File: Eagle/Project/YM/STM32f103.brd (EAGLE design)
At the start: 174.2 x 86.5 mm, 81 parts, among them IC1 YM3812, IC10 YM3812, IC11 YM3014B, IC12 OPA2134, IC14 74ALS04N, IC15 6N136, IC2 YM3014B, IC3 OPA2134, IC4 YM3812, IC5 YM3014B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

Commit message: gerber files
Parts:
- moved SL9 0.13 mm to (66.7, 9.65), flipped to the top, turned to 0 degrees
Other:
- board size 174.2 x 86.5 mm -> 174.6 x 86.4 mm
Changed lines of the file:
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@@
 <setting verticaltext="up"/>
 </settings>
-<grid distance="5" unitdist="mil" unit="mil" style="lines" multiple="1" display="yes" altdistance="5" altunitdist="mil" altunit="mil"/>
+<grid distance="25" unitdist="mil" unit="mil" style="lines" multiple="1" display="yes" altdistance="5" altunitdist="mil" altunit="mil"/>
 <layers>
 <layer number="1" name="Top" color="4" fill="1" visible="yes" active="yes"/>
@@
 <board>
 <plain>
-<wire x1="0" y1="0" x2="174.224" y2="0" width="0" layer="20" grouprefs="ASD"/>
-<wire x1="174.224" y1="0" x2="174.224" y2="86.538" width="0" layer="20" grouprefs="ASD"/>
-<wire x1="174.224" y1="86.538" x2="0" y2="86.538" width="0" layer="20" grouprefs="ASD"/>
-<wire x1="0" y1="86.538" x2="0" y2="0" width="0" layer="20"/>
+<wire x1="0" y1="0" x2="174.625" y2="0" width="0" layer="20" grouprefs="ASD"/>
+<wire x1="174.625" y1="0" x2="174.625" y2="86.36" width="0" layer="20" grouprefs="ASD"/>
+<wire x1="174.625" y1="86.36" x2="0" y2="86.36" width="0" layer="20" grouprefs="ASD"/>
+<wire x1="0" y1="86.36" x2="0" y2="0" width="0" layer="20"/>
 <hole x="172.212" y="84.582" drill="3.2004"/>
 <hole x="172.212" y="2.032" drill="3.2004"/>
@@
 <attribute name="VALUE" x="32.004" y="15.2146" size="1.27" layer="27" ratio="10"/>
 </element>
-<element name="SL9" library="con-amp-quick" library_urn="urn:adsk.eagle:library:125" package="06P" package3d_urn="urn:adsk.eagle:package:5960/1" value="" x="66.675" y="9.525" smashed="yes" rot="MR180">
-<attribute name="MF" value="" x="66.675" y="9.525" size="1.778" layer="28" rot="MR180" display="off"/>
-<attribute name="MPN" value="" x="66.675" y="9.525" size="1.778" layer="28" rot="MR180" display="off"/>
-<attribute name="NAME" x="59.436" y="12.2174" size="1.27" layer="25" ratio="10"/>
-<attribute name="OC_FARNELL" value="unknown" x="66.675" y="9.525" size="1.778" layer="28" rot="MR180" display="off"/>
-<attribute name="OC_NEWARK" value="unknown" x="66.675" y="9.525" size="1.778" layer="28" rot="MR180" display="off"/>
-<attribute name="POPULARITY" value="5" x="66.675" y="9.525" size="1.778" layer="28" rot="MR180" display="off"/>
-<attribute name="VALUE" x="59.309" y="13.3604" size="1.27" layer="28" ratio="10" rot="MR180"/>
+<element name="SL9" library="con-amp-quick" library_urn="urn:adsk.eagle:library:125" package="06P" package3d_urn="urn:adsk.eagle:package:5960/1" value="" x="66.675" y="9.652" smashed="yes">
+<attribute name="MF" value="" x="66.675" y="9.652" size="1.778" layer="27" display="off"/>
+<attribute name="MPN" value="" x="66.675" y="9.652" size="1.778" layer="27" display="off"/>
+<attribute name="NAME" x="59.436" y="12.4714" size="1.27" layer="25" ratio="10"/>
+<attribute name="OC_FARNELL" value="unknown" x="66.675" y="9.652" size="1.778" layer="27" display="off"/>
+<attribute name="OC_NEWARK" value="unknown" x="66.675" y="9.652" size="1.778" layer="27" display="off"/>
+<attribute name="POPULARITY" value="5" x="66.675" y="9.652" size="1.778" layer="27" display="off"/>
+<attribute name="VALUE" x="59.309" y="5.8166" size="1.27" layer="27" ratio="10"/>
 </element>
 </elements>
@@
 <wire x1="65.405" y1="12.827" x2="67.437" y2="12.827" width="0.2032" layer="1"/>
 <contactref element="SL9" pad="4"/>
-<wire x1="67.945" y1="12.319" x2="67.945" y2="9.525" width="0.2032" layer="1"/>
-<wire x1="67.437" y1="12.827" x2="67.945" y2="12.319" width="0.2032" layer="1"/>
-<wire x1="67.945" y1="7.112" x2="67.945" y2="9.525" width="0.2032" layer="1"/>
+<wire x1="67.945" y1="12.319" x2="67.437" y2="12.827" width="0.2032" layer="1"/>
+<wire x1="67.945" y1="9.652" x2="67.945" y2="12.319" width="0.2032" layer="1"/>
+<wire x1="67.945" y1="9.652" x2="67.945" y2="7.112" width="0.2032" layer="1"/>
 </signal>
 <signal name="EXP-SPI-MISO">
@@
 <wire x1="100.7745" y1="4.6355" x2="67.8815" y2="4.6355" width="0.2032" layer="1"/>
 <wire x1="67.8815" y1="4.6355" x2="65.405" y2="7.112" width="0.2032" layer="1"/>
-<wire x1="60.198" y1="17.567025" x2="65.425" y2="12.340025" width="0.2032" layer="1"/>
+<wire x1="65.405" y1="12.360025" x2="60.198" y2="17.567025" width="0.2032" layer="1"/>
 <contactref element="SL9" pad="3"/>
-<wire x1="65.425" y1="12.340025" x2="65.425" y2="9.545" width="0.2032" layer="1"/>
-<wire x1="65.425" y1="9.545" x2="65.405" y2="9.525" width="0.2032" layer="1"/>
-<wire x1="65.405" y1="7.112" x2="65.405" y2="9.525" width="0.2032" layer="1"/>
+<wire x1="65.405" y1="7.112" x2="65.405" y2="9.652" width="0.2032" layer="1"/>
+<wire x1="65.405" y1="9.652" x2="65.405" y2="12.360025" width="0.2032" layer="1"/>
 </signal>
 <signal name="EXP-SPI-CLK">
@@
 <wire x1="100.965" y1="4.2672" x2="65.8368" y2="4.2672" width="0.2032" layer="1"/>
 <wire x1="65.8368" y1="4.2672" x2="62.992" y2="7.112" width="0.2032" layer="1"/>
-<wire x1="62.992" y1="7.112" x2="62.925" y2="7.179" width="0.2032" layer="1"/>
 <wire x1="102.108" y1="9.906" x2="101.219" y2="10.795" width="0.2032" layer="1"/>
 <wire x1="101.219" y1="10.795" x2="100.33" y2="10.795" width="0.2032" layer="1"/>
 <contactref element="SL9" pad="2"/>
-<wire x1="62.865" y1="14.43305" x2="62.865" y2="9.525" width="0.2032" layer="1"/>
-<wire x1="62.925" y1="7.179" x2="62.865" y2="7.239" width="0.2032" layer="1"/>
-<wire x1="62.865" y1="7.239" x2="62.865" y2="9.525" width="0.2032" layer="1"/>
+<wire x1="62.865" y1="14.43305" x2="62.865" y2="9.652" width="0.2032" layer="1"/>
+<wire x1="62.992" y1="7.112" x2="62.865" y2="7.239" width="0.2032" layer="1"/>
+<wire x1="62.865" y1="7.239" x2="62.865" y2="9.652" width="0.2032" layer="1"/>
 </signal>
 <signal name="YM2-CS">
@@
 <wire x1="57.023" y1="29.083" x2="57.023" y2="5.207" width="0.3048" layer="16"/>
 <wire x1="57.023" y1="5.207" x2="58.039" y2="4.191" width="0.3048" layer="16"/>
-<wire x1="67.945" y1="4.191" x2="58.039" y2="4.191" width="0.3048" layer="16"/>
-<wire x1="72.905" y1="4.191" x2="85.979" y2="4.191" width="0.3048" layer="16"/>
+<wire x1="67.691" y1="4.191" x2="58.039" y2="4.191" width="0.3048" layer="16"/>
 <wire x1="85.979" y1="4.191" x2="87.63" y2="5.842" width="0.3048" layer="16"/>
 <wire x1="87.63" y1="5.842" x2="87.63" y2="8.255" width="0.3048" layer="16"/>
@@
 <wire x1="28.067" y1="77.597" x2="25.654" y2="80.01" width="0.3048" layer="16"/>
 <contactref element="SL9" pad="5"/>
-<wire x1="70.425" y1="9.465" x2="70.425" y2="6.671" width="0.3048" layer="16"/>
-<wire x1="70.425" y1="9.465" x2="70.485" y2="9.525" width="0.3048" layer="16"/>
-<wire x1="70.425" y1="6.671" x2="67.945" y2="4.191" width="0.3048" layer="16"/>
-<wire x1="70.425" y1="6.671" x2="72.905" y2="4.191" width="0.3048" layer="16"/>
+<wire x1="67.691" y1="4.191" x2="70.485" y2="6.985" width="0.3048" layer="16"/>
+<wire x1="70.485" y1="6.985" x2="70.485" y2="9.652" width="0.3048" layer="16"/>
+<wire x1="70.485" y1="6.985" x2="73.279" y2="4.191" width="0.3048" layer="16"/>
+<wire x1="73.279" y1="4.191" x2="85.979" y2="4.191" width="0.3048" layer="16"/>
 </signal>
 <signal name="N$3">
@@
 <wire x1="59.2236" y1="54.924" x2="59.5376" y2="54.61" width="0.2032" layer="1"/>
 <wire x1="59.5376" y1="54.61" x2="59.5376" y2="17.293475" width="0.2032" layer="1"/>
-<wire x1="59.5376" y1="17.293475" x2="60.3230375" y2="16.5080375" width="0.2032" layer="1"/>
 <contactref element="SL9" pad="1"/>
-<wire x1="60.3230375" y1="16.5080375" x2="60.3230375" y2="9.5269625" width="0.2032" layer="1"/>
-<wire x1="60.3230375" y1="9.5269625" x2="60.325" y2="9.525" width="0.2032" layer="1"/>
+<wire x1="60.325" y1="16.506075" x2="60.325" y2="9.652" width="0.2032" layer="1"/>
+<wire x1="59.5376" y1="17.293475" x2="60.325" y2="16.506075" width="0.2032" layer="1"/>
 </signal>
 <signal name="N$15">

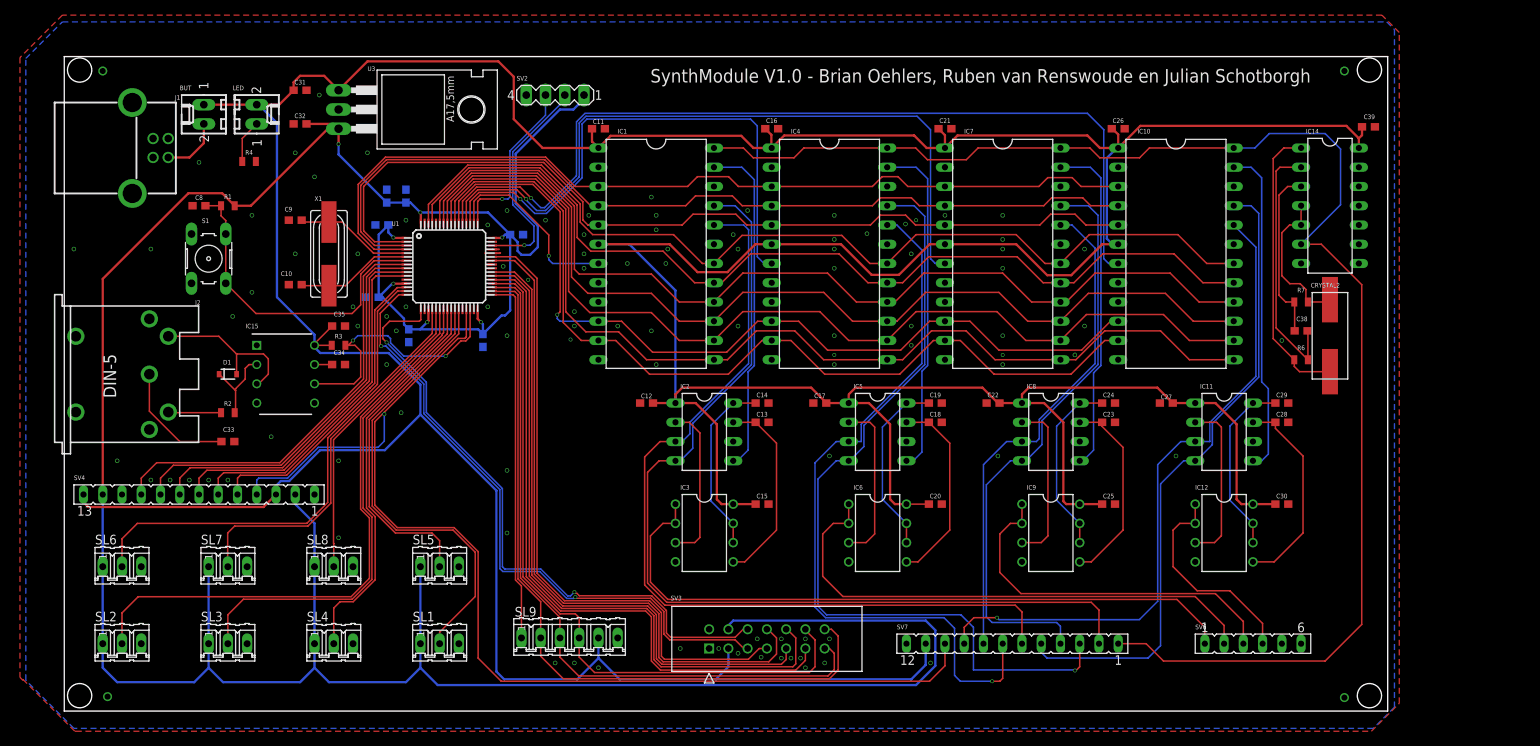
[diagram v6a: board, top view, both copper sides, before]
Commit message: Randen en holes op mm grid
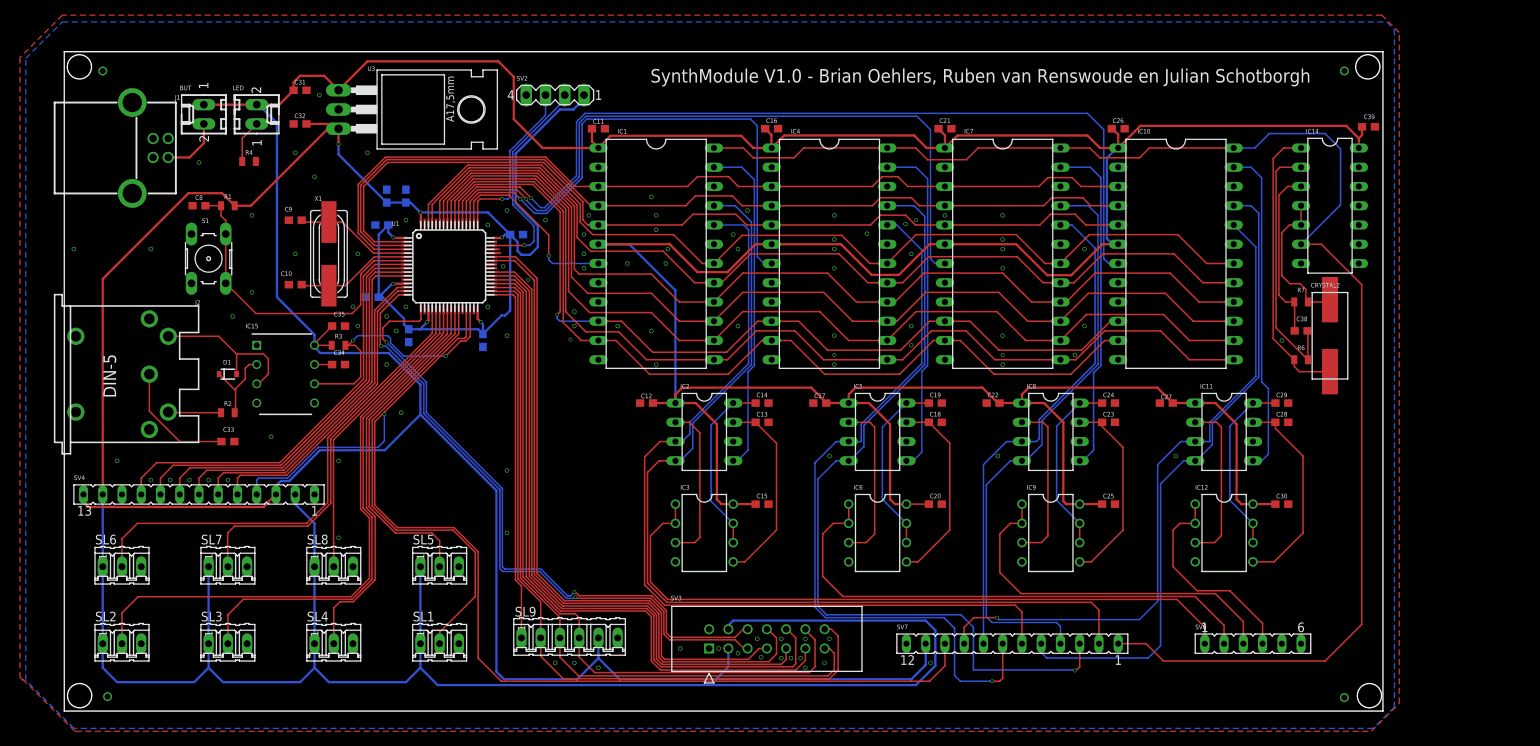
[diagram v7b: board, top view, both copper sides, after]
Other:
- board size 174.6 x 86.4 mm -> 174 x 87 mm
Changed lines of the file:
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@@
 <setting verticaltext="up"/>
 </settings>
-<grid distance="25" unitdist="mil" unit="mil" style="lines" multiple="1" display="yes" altdistance="5" altunitdist="mil" altunit="mil"/>
+<grid distance="1" unitdist="mm" unit="mm" style="lines" multiple="1" display="yes" altdistance="5" altunitdist="mil" altunit="mil"/>
 <layers>
 <layer number="1" name="Top" color="4" fill="1" visible="yes" active="yes"/>
@@
 <board>
 <plain>
-<wire x1="0" y1="0" x2="174.625" y2="0" width="0" layer="20" grouprefs="ASD"/>
-<wire x1="174.625" y1="0" x2="174.625" y2="86.36" width="0" layer="20" grouprefs="ASD"/>
-<wire x1="174.625" y1="86.36" x2="0" y2="86.36" width="0" layer="20" grouprefs="ASD"/>
-<wire x1="0" y1="86.36" x2="0" y2="0" width="0" layer="20"/>
-<hole x="172.212" y="84.582" drill="3.2004"/>
+<wire x1="0" y1="0" x2="174" y2="0" width="0" layer="20" grouprefs="ASD"/>
+<wire x1="174" y1="0" x2="174" y2="87" width="0" layer="20" grouprefs="ASD"/>
+<wire x1="174" y1="87" x2="0" y2="87" width="0" layer="20" grouprefs="ASD"/>
+<wire x1="0" y1="87" x2="0" y2="0" width="0" layer="20"/>
+<hole x="172" y="85" drill="3.2004"/>
 <hole x="172.212" y="2.032" drill="3.2004"/>
-<hole x="2.032" y="84.582" drill="3.2004"/>
+<hole x="2" y="85" drill="3.2004"/>
 <hole x="2.032" y="2.032" drill="3.2004"/>
 <text x="77.343" y="82.931" size="1.778" layer="25">SynthModule V1.0 - Brian Oehlers, Ruben van Renswoude en Julian Schotborgh</text>
